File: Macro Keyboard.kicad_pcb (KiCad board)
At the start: 2 copper layers, 101.6 x 123.4 mm, 137 parts, among them J2901 FPC 1x24, Q2901 Q_PJFET_GDS, SW1001 KH-PS1611-54, SW1101 KH-PS1611-54, SW1201 KH-PS1611-54, SW1301 KH-PS1611-54, SW1401 KH-PS1611-54, SW1501 KH-PS1611-54, SW2801 SWITCH TACTILE SPST-NO 50MA 1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, SW601 KH-PS1611-54, SW701 KH-PS1611-54, SW801 KH-PS1611-54, SW901 KH-PS1611-54, U2701 PCA9745BTWJ, U2801 Pico-JER, U301 VEML7700, U401 PI4ULS5V201TAEX

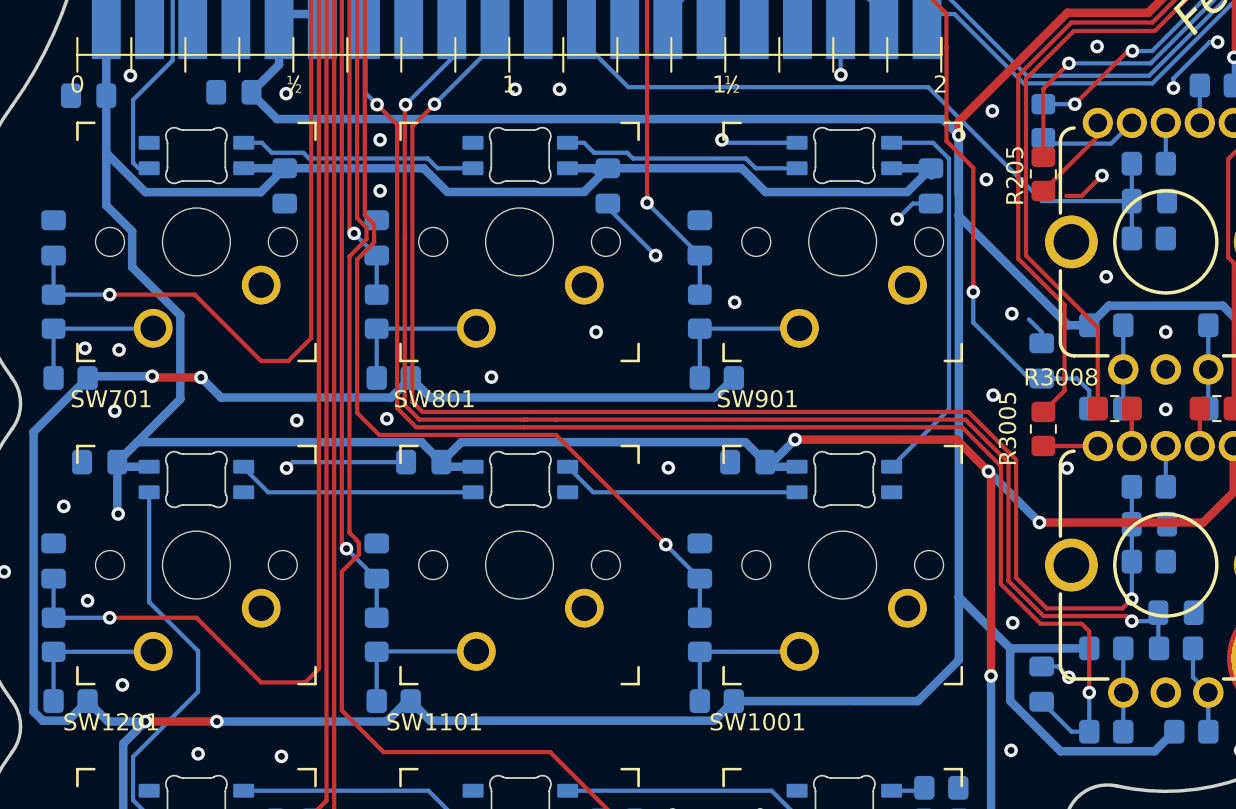
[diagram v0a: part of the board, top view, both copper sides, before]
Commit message: Added estop stp and Marks comments from DFM check
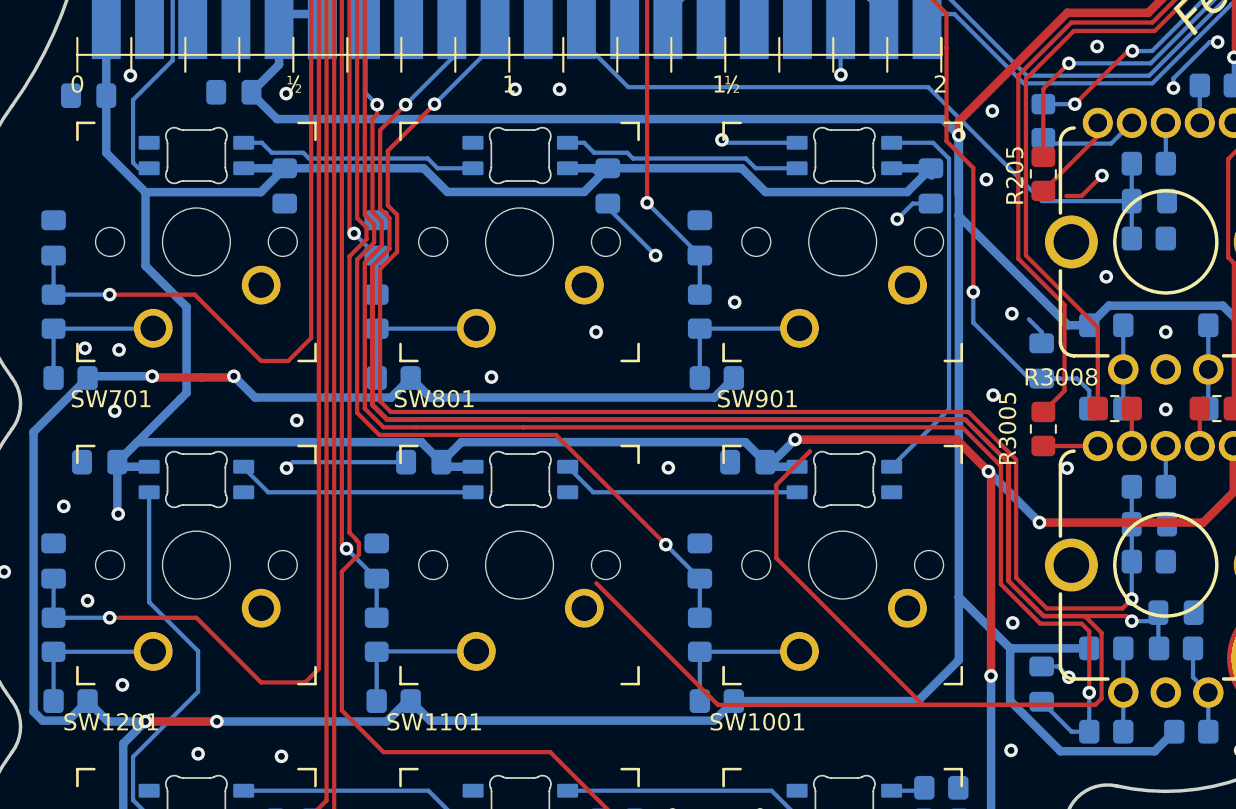
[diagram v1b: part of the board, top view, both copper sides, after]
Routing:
- net /REnc_2_B: track 80.1 -> 216.7 mm
- net /REnc_2_SW: track 83.0 -> 86.2 mm
- net +5V: track 343.4 -> 340.4 mm
- net /REnc_2_A: track 83.6 -> 85.8 mm
- net GND: vias 110 -> 107

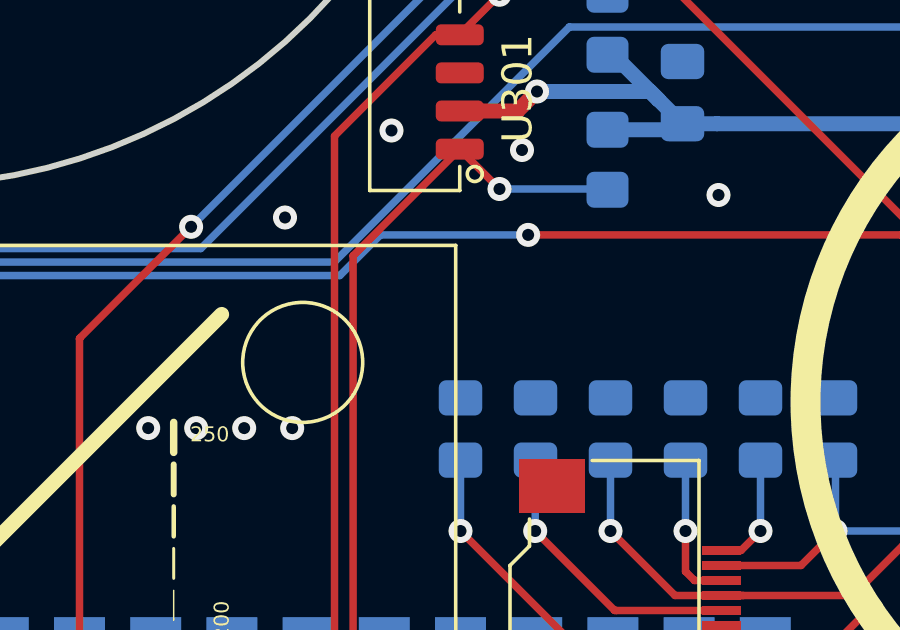
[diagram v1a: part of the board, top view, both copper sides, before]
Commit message: Add JLC P/N locator text
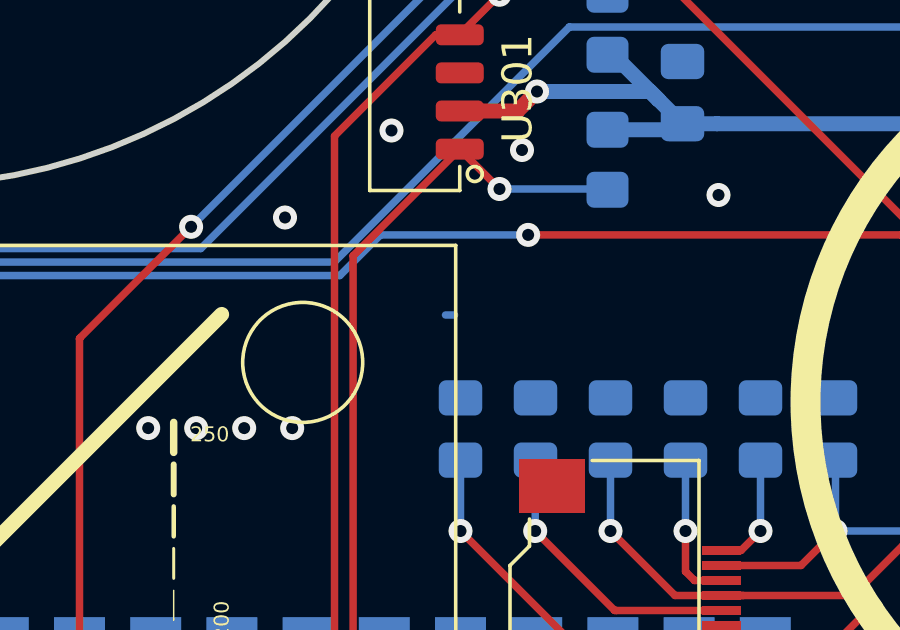
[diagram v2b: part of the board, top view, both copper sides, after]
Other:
- board text added: "JLCJLCJLCJLC"

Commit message: Fix design error in PI4ULS5V201TAEX. Reset and reassigned all annotations.
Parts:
- removed U401: PI4ULS5V201TAEX, Package_TO_SOT_SMD:SOT-23-6
- added R301: 4.7k 5%, Resistor_SMD:R_0805_2012Metric_Pad1.20x1.40mm_HandSolder, B.Cu at (136.9, 49.0)
- added U301: PI4ULS5V201TAEX, Package_TO_SOT_SMD:SOT-23-6, B.Cu at (132.9, 52.3)
- renumbered C1101 to C1001, C1201 to C1101, C1301 to C1201, C1401 to C1301, C1501 to C1401, C1701 to C1601, C1801 to C1701, C1901 to C1801, C2001 to C1901, C2101 to C2001, C301 to C201, C2201 to C2101, C2301 to C2201, C2401 to C2301, C2501 to C2401, C2601 to C2501, C2701 to C2601, C2901 to C2701, C2902 to C2702, C2903 to C2703, C2904 to C2704, C2906 to C2705, C2907 to C2706, C2908 to C2707, C2909 to C2708, C2905 to C2709, C3001 to C2801, C3002 to C2802, C3003 to C2803, C201 to C2901, C202 to C2902, C203 to C2903, C2801 to C3001, C2802 to C3002, C401 to C301, C402 to C302, C601 to C501, C701 to C601, C801 to C701, C901 to C801, C1001 to C901, D1701 to D1601, D1801 to D1701, D1901 to D1801, D2001 to D1901, D2101 to D2001, D2201 to D2101, D2301 to D2201, D2401 to D2301, D2501 to D2401, D2601 to D2501, D2901 to D2701, D2902 to D2702, D2903 to D2703, J2901 to J2701, L2901 to L2701, Q2901 to Q2701, R1101 to R1001, R1102 to R1002, R1201 to R1101, R1202 to R1102, R1301 to R1201, R1302 to R1202, R1401 to R1301, R1402 to R1302, R1501 to R1401, R1502 to R1402, R1601 to R1501, R1602 to R1502, R301 to R201, R302 to R202, R2701 to R2601, R2702 to R2602, R2703 to R2603, R2704 to R2604, R2705 to R2605, R2706 to R2606, R2707 to R2607, R2901 to R2701, R2902 to R2702, R3001 to R2801, R3002 to R2802, R3003 to R2803, R3004 to R2804, R3006 to R2805, R3007 to R2806, R3005 to R2807, R3008 to R2808, R3009 to R2809, R201 to R2901, R202 to R2902, R203 to R2903, R204 to R2904, R206 to R2905, R207 to R2906, R205 to R2907, R208 to R2908, R209 to R2909, R2801 to R3001, R601 to R501, R602 to R502, R701 to R601, R702 to R602, R801 to R701, R802 to R702, R901 to R801, R902 to R802, R1001 to R901, R1002 to R902, S3001 to S2801, S201 to S2901, SW1101 to SW1001, SW1201 to SW1101, SW1301 to SW1201, SW1401 to SW1301, SW1501 to SW1401, SW2801 to SW3001, SW601 to SW501, SW701 to SW601, SW801 to SW701, SW901 to SW801, SW1001 to SW901, U301 to U201, U2701 to U2601, U2801 to U3001
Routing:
- net Net-(R301-Pad1): track 0.00 -> 12.1 mm, vias 0 -> 2
- net +5V: track 340.4 -> 345.4 mm
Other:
- board text added: "P/N: 21-11.03-3 REV: A.R0 S/N:"
- board text removed: "P/N: 21-11.03-3 REV: - S/N:"

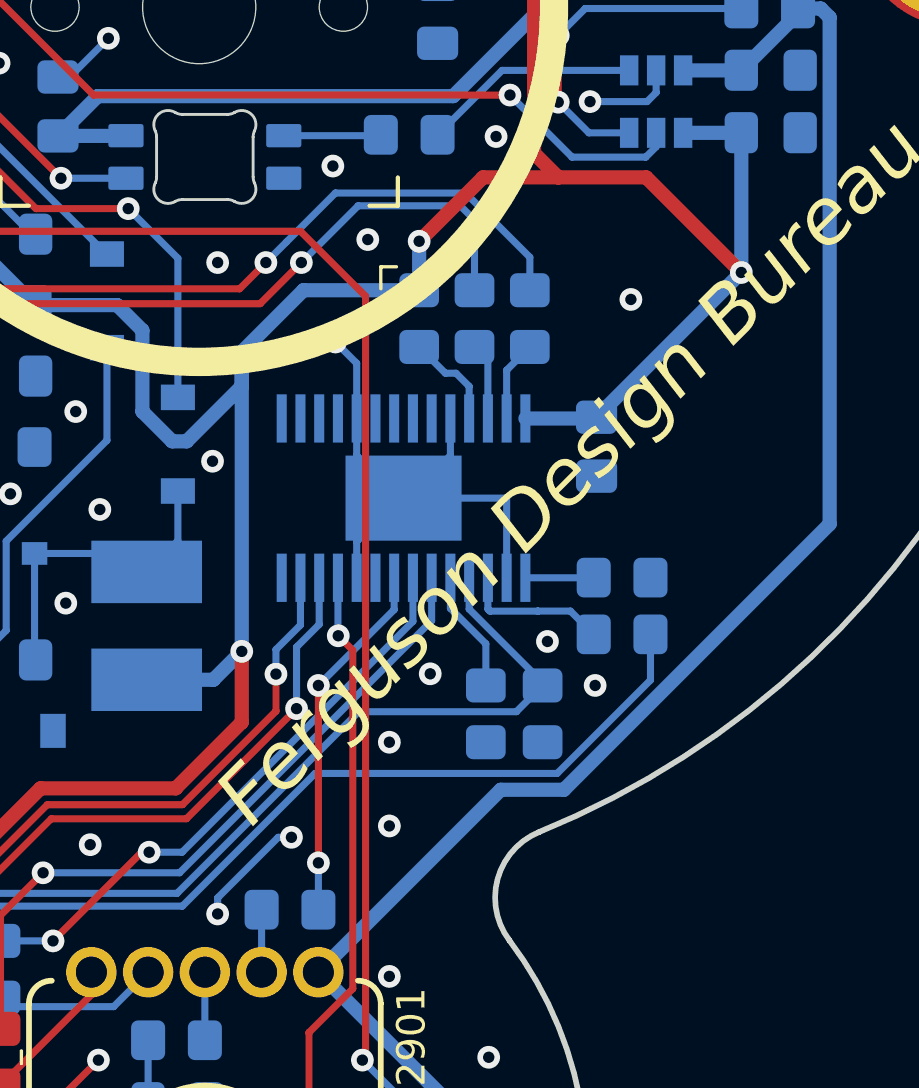
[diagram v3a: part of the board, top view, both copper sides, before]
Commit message: Remove resistor for SPI MOSI, MISO, and CS for LED Driver
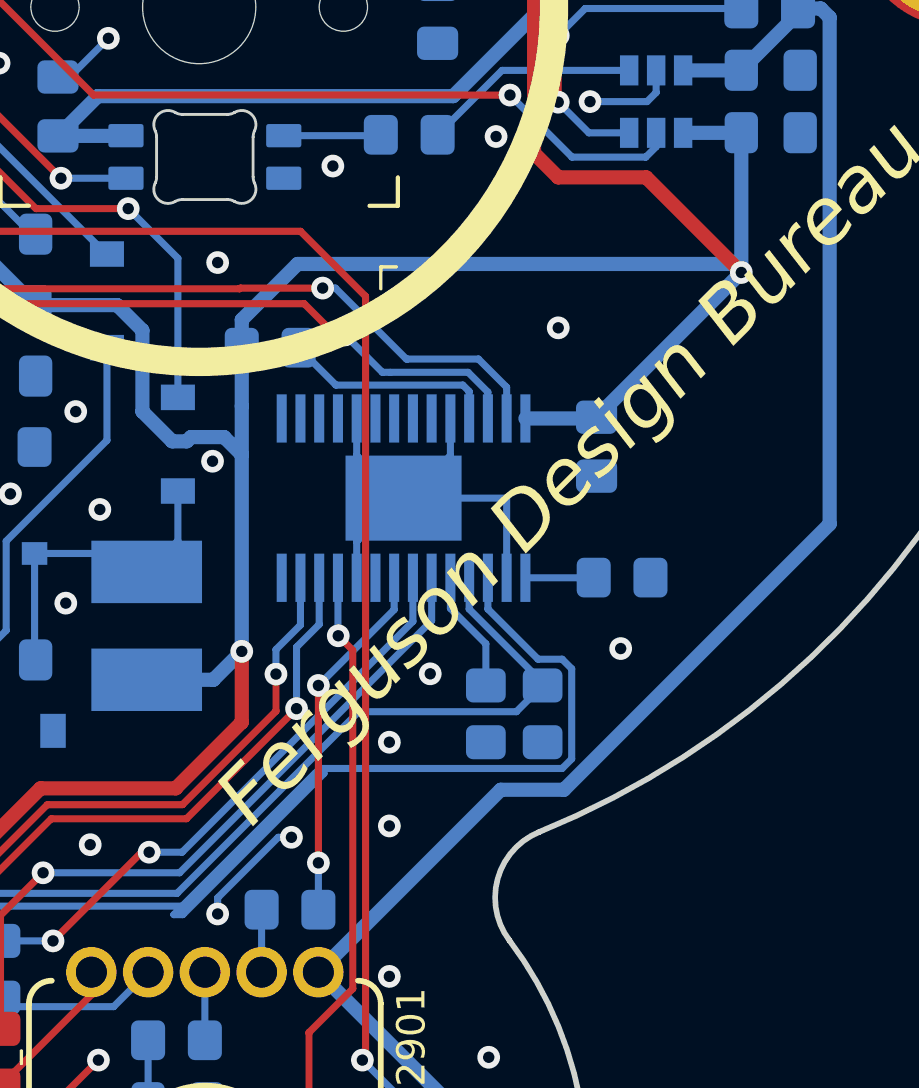
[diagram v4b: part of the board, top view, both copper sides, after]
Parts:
- removed R2604, R2606, R2607: 1k 5%, Resistor_SMD:R_0805_2012Metric_Pad1.20x1.40mm_HandSolder
- moved R2605 5.35 mm to (119.3, 61.0), turned to 0 degrees
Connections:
- U2601 pad 26: Net-(R2607-Pad2) -> SPI_SCLK_3V
- U2601 pad 27: Net-(R2606-Pad2) -> SPI_MOSI_3V
- U2601 pad 3: Net-(R2604-Pad1) -> SPI_MISO_3V
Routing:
- net SPI_MISO_3V: track 36.3 -> 53.6 mm
- net Net-(R2604-Pad1): track 5.20 -> 0.00 mm
- net Net-(R2605-Pad2): track 3.47 -> 7.60 mm
- net +3V3: track 480.4 -> 484.3 mm, vias 13 -> 12
- net GND: track 82.9 -> 79.9 mm, vias 107 -> 104
- net Net-(R2606-Pad2): track 2.86 -> 0.00 mm
- net Net-(R2607-Pad2): track 2.71 -> 0.00 mm
- net SPI_MOSI_3V: track 54.0 -> 52.3 mm
- net SPI_SCLK_3V: track 52.4 -> 50.9 mm
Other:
- board text added: "P/N: 21-11.03-3 REV: A.R1 S/N:"
- board text removed: "P/N: 21-11.03-3 REV: A.R0 S/N:"

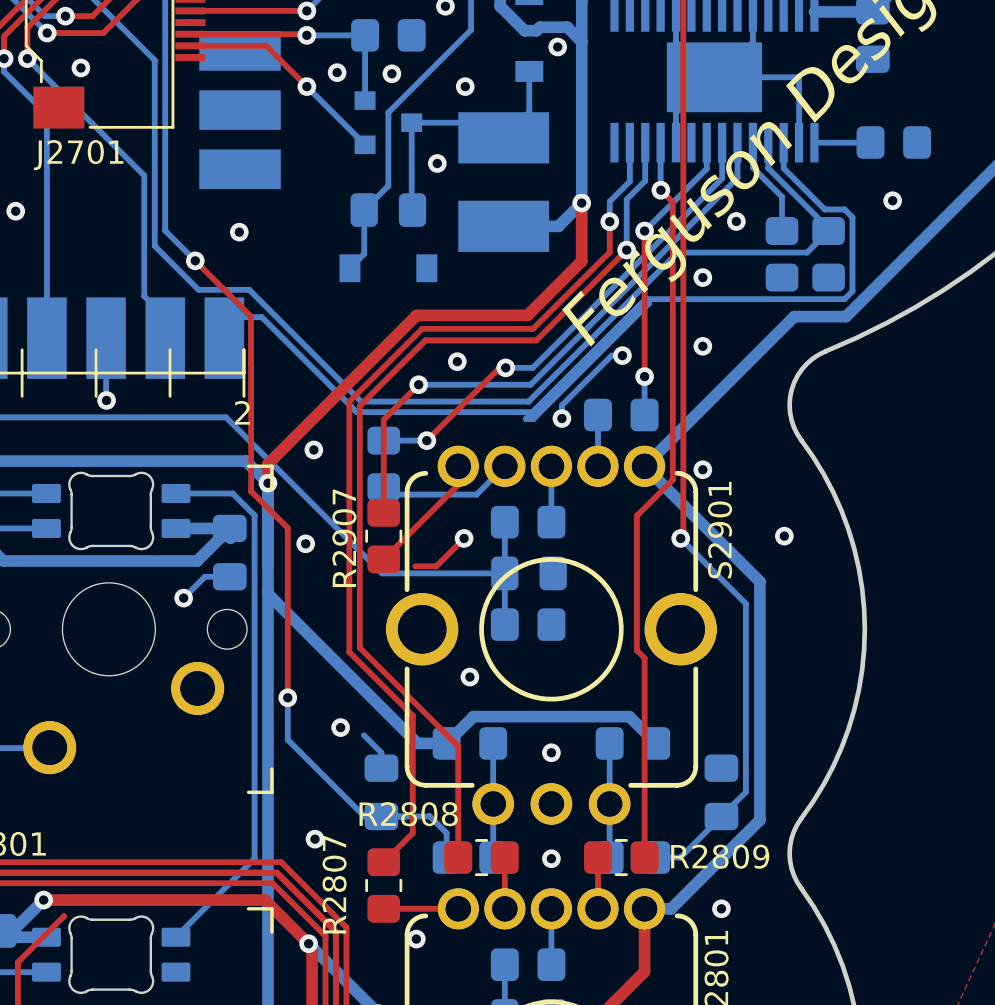
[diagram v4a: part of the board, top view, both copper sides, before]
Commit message: Fixed wiring for rotary encoder 2. R and B pins were swapped.
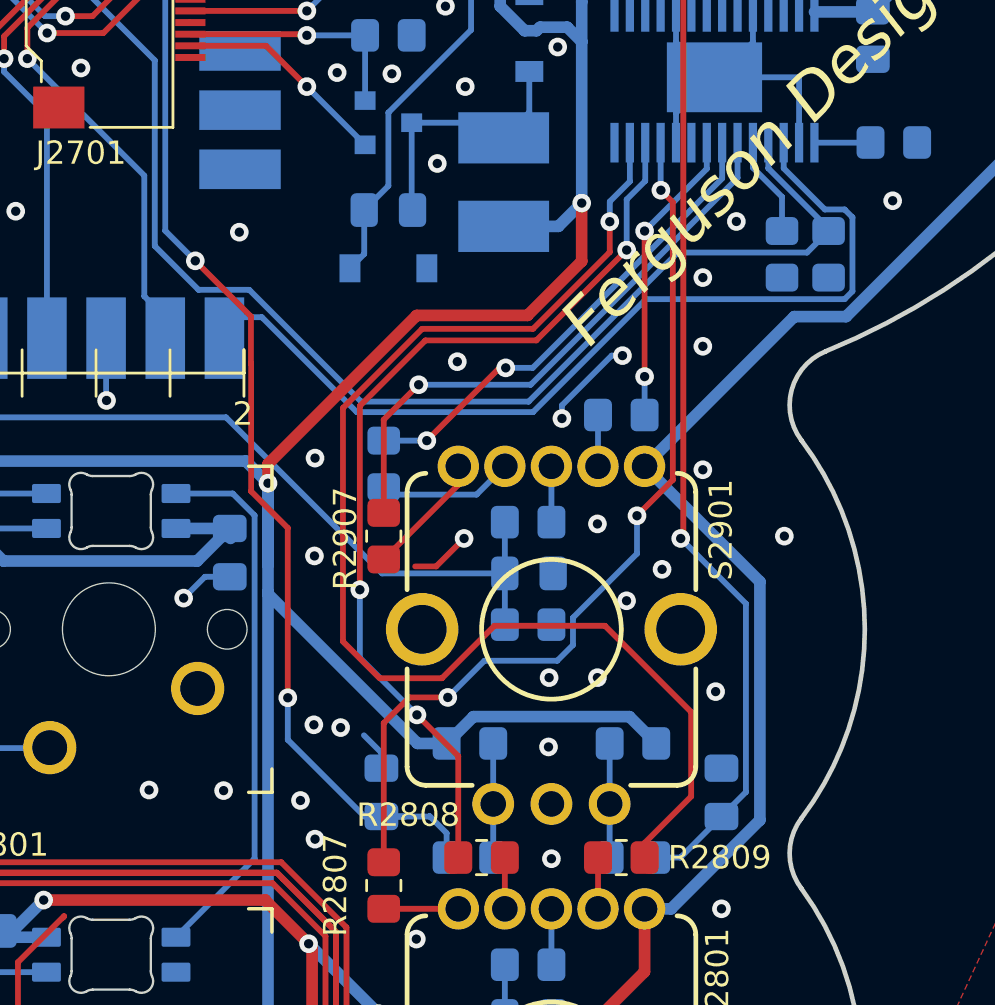
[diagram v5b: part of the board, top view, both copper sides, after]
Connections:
- R2807 pad 1: /RGB Driver/DRIVER_LED_SW2_B_5V -> /RGB Driver/DRIVER_LED_SW2_R_5V
- R2809 pad 1: /RGB Driver/DRIVER_LED_SW2_R_5V -> /RGB Driver/DRIVER_LED_SW2_B_5V
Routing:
- net SPI_MISO_3V: track 53.6 -> 38.9 mm
- net /RGB Driver/DRIVER_LED_SW2_B_5V: track 40.3 -> 54.5 mm
- net /RGB Driver/DRIVER_LED_SW2_R_5V: track 31.7 -> 39.6 mm, vias 1 -> 3
- net GND: vias 104 -> 113
- net /RGB Driver/DRIVER_LED_SW2_G_5V: vias 1 -> 3
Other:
- board text added: "P/N: 21-11.03-3 REV: A.R2 S/N:"
- board text removed: "P/N: 21-11.03-3 REV: A.R1 S/N:"

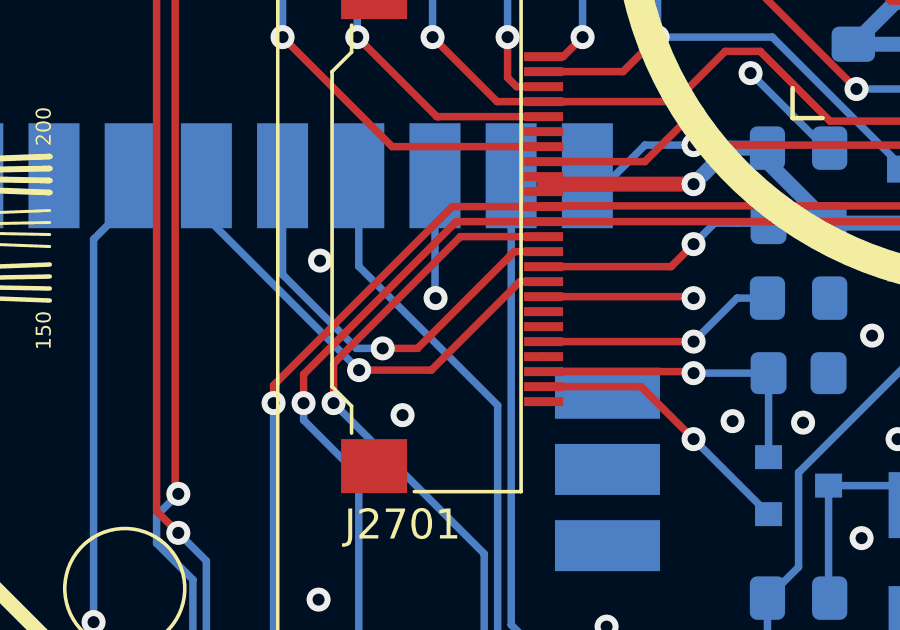
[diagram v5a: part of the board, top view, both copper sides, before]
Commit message: Assignments for Pico GPIO 11 and 12 were flipped. Fixed.
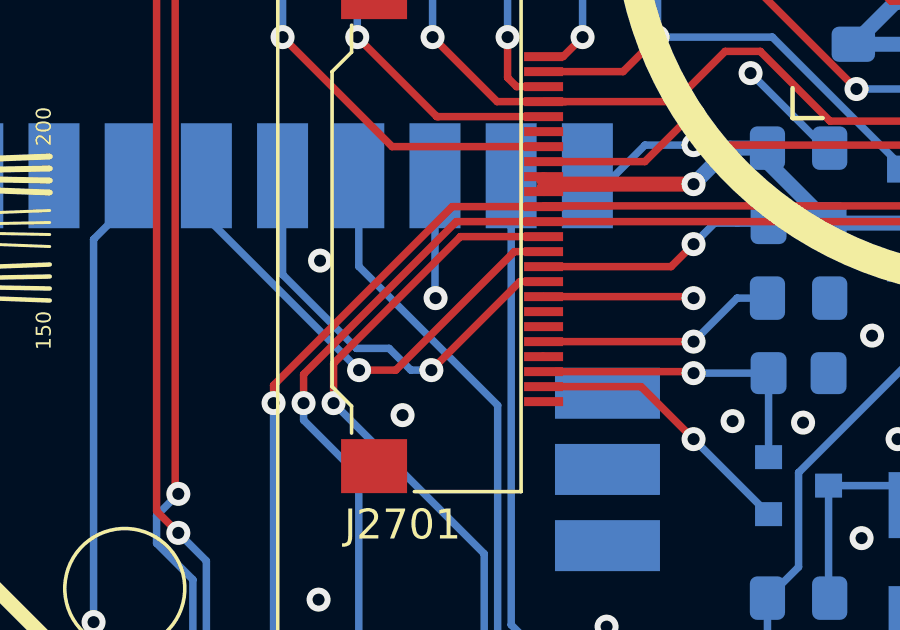
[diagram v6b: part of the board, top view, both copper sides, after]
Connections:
- U3001 pad 15: /DS_BUSY_3V3 -> /DS_D_C_3V3
- U3001 pad 16: /DS_D_C_3V3 -> /DS_BUSY_3V3
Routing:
- net /DS_D_C_3V3: track 13.4 -> 15.5 mm
- net /DS_BUSY_3V3: track 15.1 -> 13.6 mm
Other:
- board text added: "P/N: 21-11.03-3 REV: A.R3 S/N:"
- board text removed: "P/N: 21-11.03-3 REV: A.R2 S/N:"

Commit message: R2701 should be 0.47 ohm...not 470 ohm
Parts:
- R2701: value 470 5% -> 0.47 5%
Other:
- board text added: "P/N: 21-11.03-3 REV: A.R4 S/N:"
- board text removed: "P/N: 21-11.03-3 REV: A.R3 S/N:"
